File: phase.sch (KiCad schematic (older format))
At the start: 26 parts, among them U4 INA240A1PW, U5 UCC21520DW

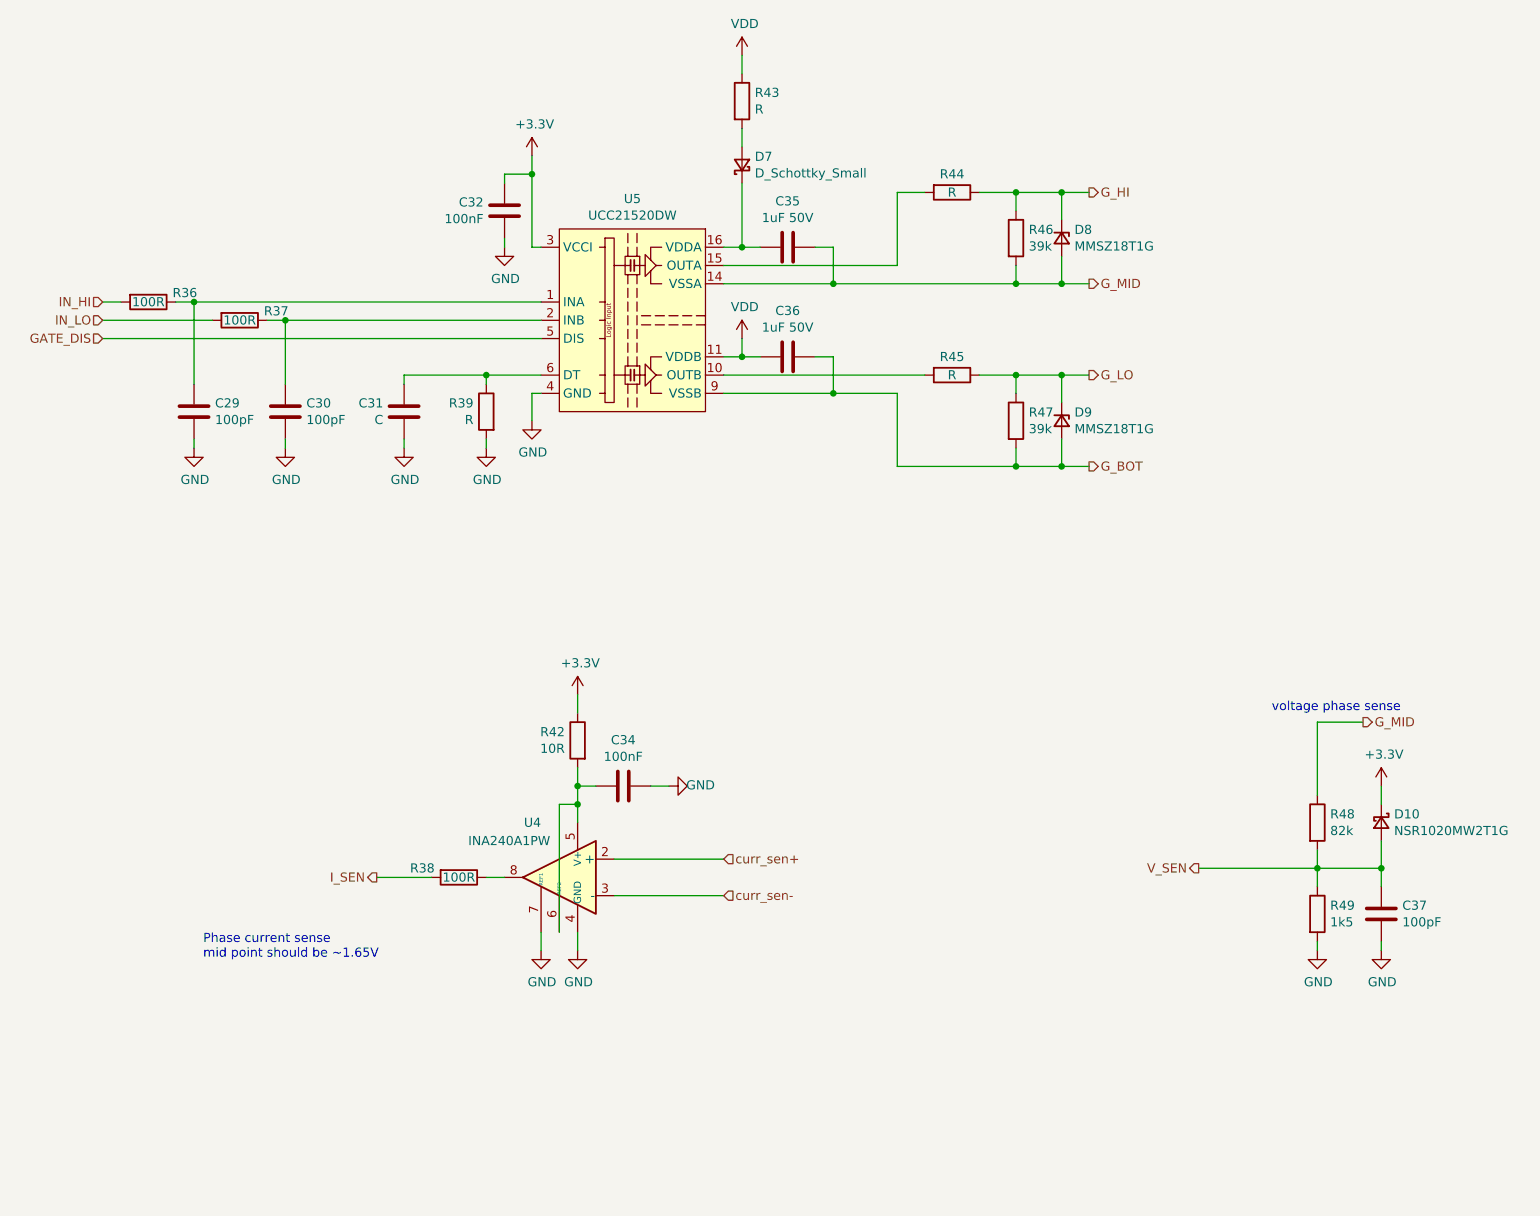
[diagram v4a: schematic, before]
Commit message: Cleaned up the schematic
Also regenerated the pdf & set boot diodes to SOD128.
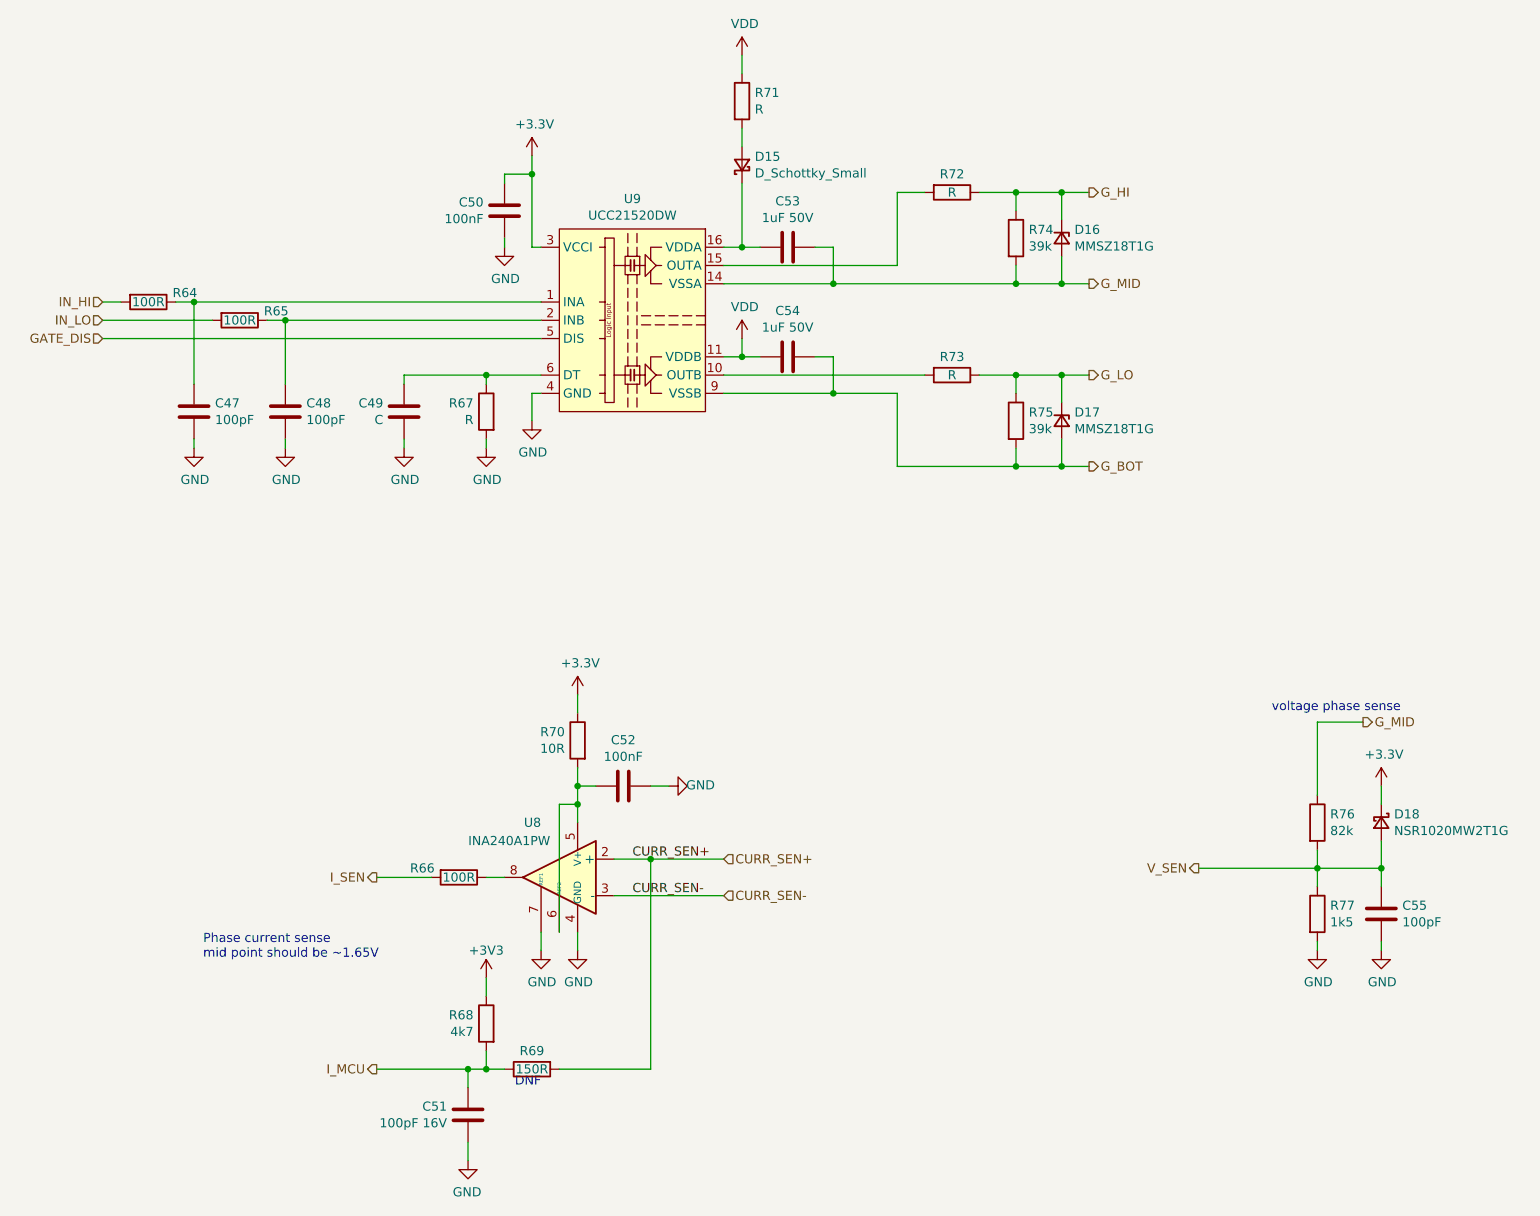
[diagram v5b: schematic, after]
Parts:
- added C33: 100pF 16V, Capacitor_SMD:C_0402_1005Metric, symbol Device:C
- added R40: 4k7, Resistor_SMD:R_0402_1005Metric, symbol Device:R
- added R41: 150R, Resistor_SMD:R_0402_1005Metric, symbol Device:R
- D7: footprint Diode_SMD:D_SMB -> Diode_SMD:D_SOD-128
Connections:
- net +3V3: now also R40.1
- net GND: now also C33.2
- net curr_sen+ renamed CURR_SEN+
- net CURR_SEN+: now also R41.2
- net curr_sen- renamed CURR_SEN-
- new net I_MCU: C33.1, R40.2, R41.1
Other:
- note added: "DNF"

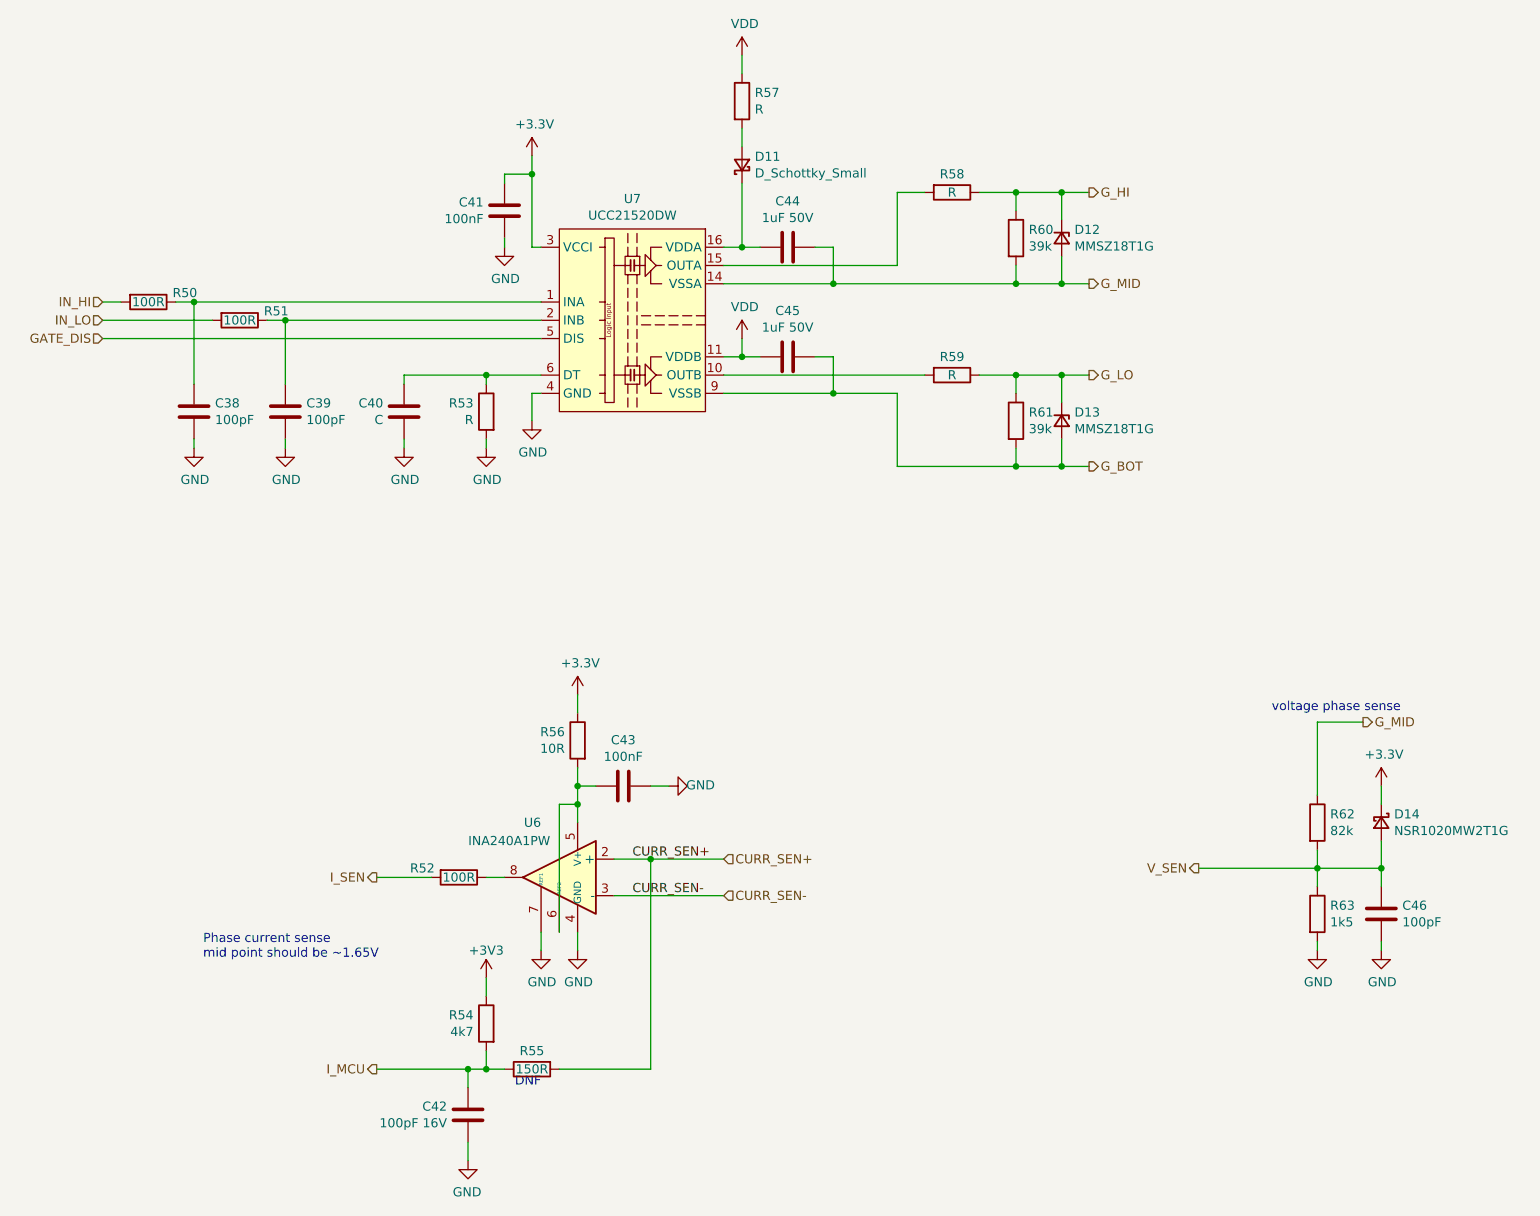
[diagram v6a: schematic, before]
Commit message: Removed coupled inductor
Added TPS61041DB
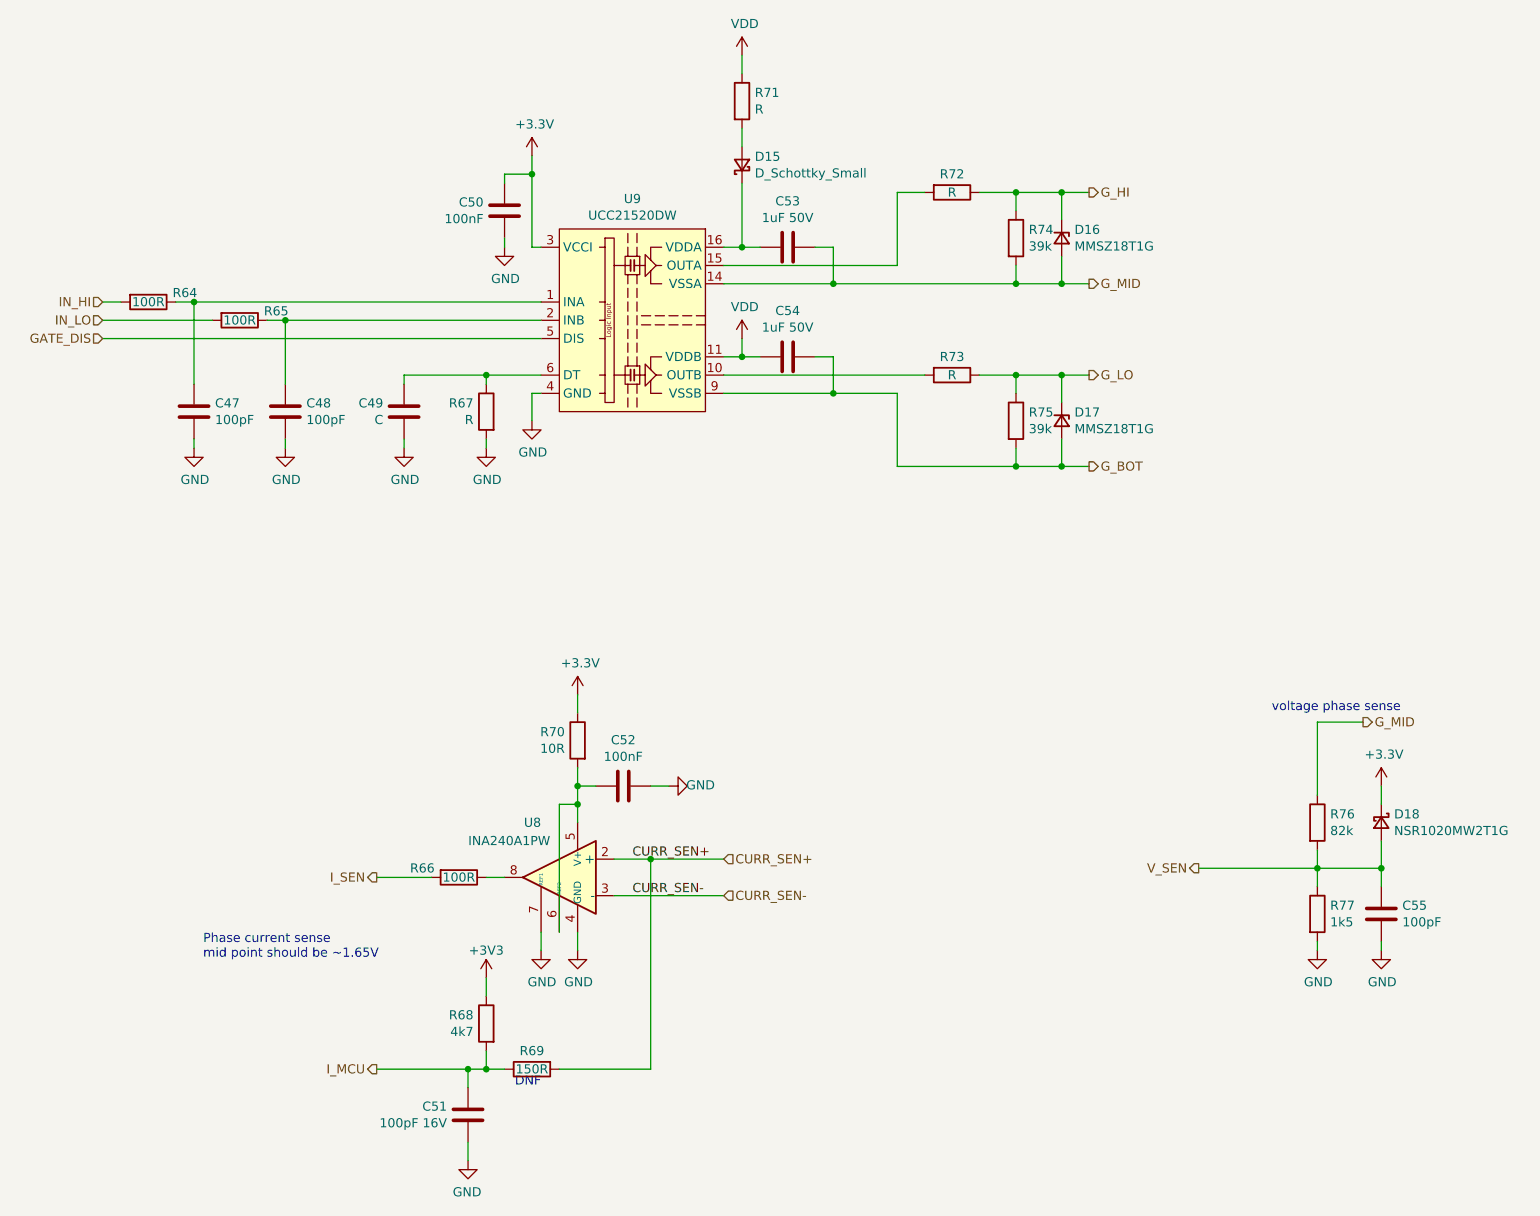
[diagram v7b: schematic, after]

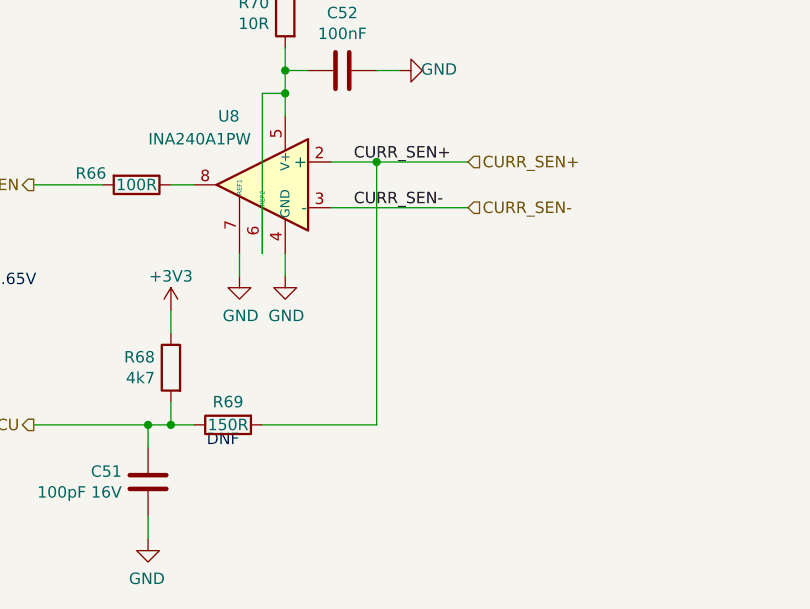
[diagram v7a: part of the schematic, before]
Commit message: Tweaking potential dividers
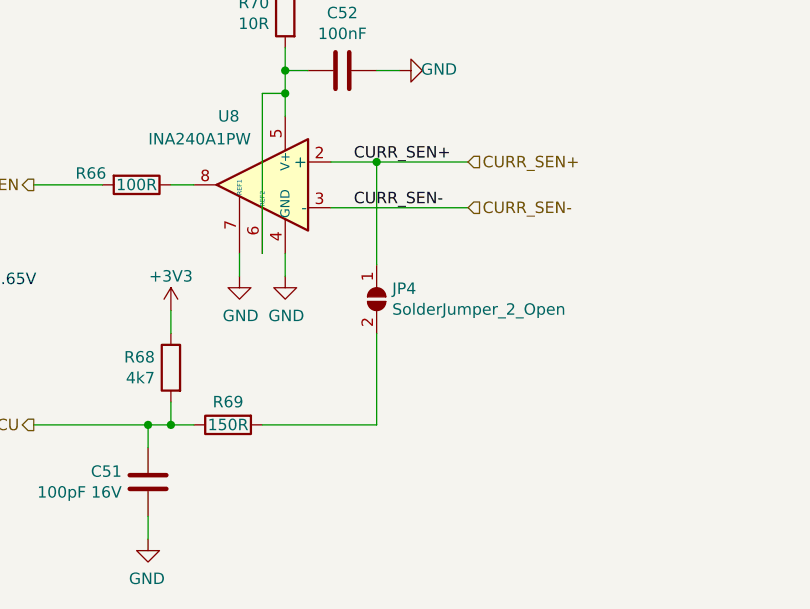
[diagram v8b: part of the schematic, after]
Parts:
- added JP2: SolderJumper_2_Open, Jumper:SolderJumper-2_P1.3mm_Open_RoundedPad1.0x1.5mm, symbol Jumper:SolderJumper_2_Open
- R48, R49: footprint Resistor_SMD:R_0402_1005Metric -> Resistor_SMD:R_0603_1608Metric
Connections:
- net CURR_SEN+: now also JP2.1 (A); no longer R41.2
- new net: JP2.2 (B), R41.2
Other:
- note removed: "DNF"
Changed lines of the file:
@@
 $Descr A4 11693 8268
 encoding utf-8
-Sheet 4 5
+Sheet 5 5
 Title "MESC_IMS_Ctrl"
 Date "2021-04-10"
@@
 F 0 "R76" H 9520 5246 50  0000 L CNN
 F 1 "82k" H 9520 5155 50  0000 L CNN
-F 2 "Resistor_SMD:R_0402_1005Metric" V 9380 5200 50  0001 C CNN
+F 2 "Resistor_SMD:R_0603_1608Metric" V 9380 5200 50  0001 C CNN
 F 3 "~" H 9450 5200 50  0001 C CNN
 F 4 "C4142" H 9450 5200 50  0001 C CNN "LCSC"
@@
 Text HLabel 8800 5450 0    50   Output ~ 0
 V_SEN
-$Comp
-L Device:R R49
-U 1 1 60742356
-P 9450 5700
-AR Path="/6070CE7F/60742356" Ref="R49"  Part="1"
-AR Path="/6074FE4E/60742356" Ref="R63"  Part="1"
-AR Path="/6075047A/60742356" Ref="R77"  Part="1"
-F 0 "R77" H 9520 5746 50  0000 L CNN
-F 1 "1k5" H 9520 5655 50  0000 L CNN
-F 2 "Resistor_SMD:R_0402_1005Metric" V 9380 5700 50  0001 C CNN
-F 3 "~" H 9450 5700 50  0001 C CNN
-F 4 "C25867" H 9450 5700 50  0001 C CNN "LCSC"
-	1    9450 5700
-	1    0    0    -1
-$EndComp
 Text Notes 3350 5950 0    50   ~ 0
 Phase current sense\nmid point should be ~~1.65V
@@
 Wire Wire Line
 	4800 7050 4800 6950
-Text Notes 5200 6650 2    50   ~ 0
-DNF
-Wire Wire Line
-	5800 6550 5800 5400
+Wire Wire Line
+	5800 6550 5800 6150
 Wire Wire Line
 	5300 6550 5800 6550
@@
 Text Label 5700 5600 0    50   ~ 0
 CURR_SEN-
+$Comp
+L Device:R R49
+U 1 1 60742356
+P 9450 5700
+AR Path="/6070CE7F/60742356" Ref="R49"  Part="1"
+AR Path="/6074FE4E/60742356" Ref="R63"  Part="1"
+AR Path="/6075047A/60742356" Ref="R77"  Part="1"
+F 0 "R77" H 9520 5746 50  0000 L CNN
+F 1 "1k5" H 9520 5655 50  0000 L CNN
+F 2 "Resistor_SMD:R_0603_1608Metric" V 9380 5700 50  0001 C CNN
+F 3 "~" H 9450 5700 50  0001 C CNN
+F 4 "C25867" H 9450 5700 50  0001 C CNN "LCSC"
+	1    9450 5700
+	1    0    0    -1
+$EndComp
+$Comp
+L Jumper:SolderJumper_2_Open JP2
+U 1 1 60924C9F
+P 5800 6000
+AR Path="/6070CE7F/60924C9F" Ref="JP2"  Part="1"
+AR Path="/6074FE4E/60924C9F" Ref="JP3"  Part="1"
+AR Path="/6075047A/60924C9F" Ref="JP4"  Part="1"
+F 0 "JP4" V 5754 6068 50  0000 L CNN
+F 1 "SolderJumper_2_Open" V 5845 6068 50  0000 L CNN
+F 2 "Jumper:SolderJumper-2_P1.3mm_Open_RoundedPad1.0x1.5mm" H 5800 6000 50  0001 C CNN
+F 3 "~" H 5800 6000 50  0001 C CNN
+F 4 "~" H 5800 6000 50  0001 C CNN "LCSC"
+	1    5800 6000
+	0    1    1    0
+$EndComp
+Wire Wire Line
+	5800 5850 5800 5400
 $EndSCHEMATC
